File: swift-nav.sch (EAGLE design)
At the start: 197 parts, among them J1 SMA, J10 RF LINK, J2 6_PIN_100MIL, J3 DEBUG HDR, J4 PIN_HDR_EDG_1.27MM_5-2, J5 RF LINK, J6 ZX62-B-5PA, J7 C-GRID-02-70543, J8 CON_UART1, J9 CON_UART3, Q1 26MHz, Q2 DDTA143, Q3 2N7002, Q5 FDT458P, SW1 B3U-1000P, SW2 B3U-1000P, SW4 B3U-1000P, U1 6SLX9FTG256, U10 MAX2769, U11 SN74LVC07A_SOIC, U12 PT7M8206B33TA5EX, U13 M25PX80, U2 LTC3407A, U3 STM32-M-64-LQFP, U7 CC1110, U8 B4050, U9 B4050, X2 ASVTX-11

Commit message: Need to add different TCXO to schematic then ready for review
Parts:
- removed C25, C26, C27, C32, C34, C35, C46: 0.1uF, rcl:C-EUC0402
- removed C33, C58: 1uF, rcl:C-EUC0402
- removed C45: 0.01uF, rcl:C-EUC0402
- removed C56: 100uF, rcl:C-EUC1210K
- removed C57: 1pF, rcl:C-EUC0402
- removed C64: DNP, rcl:C-EUC0402
- removed C65: 1.5pF, rcl:C-EUC0402
- removed C68: 100pF, rcl:C-EUC0402
- removed C69, C70: 33pF, rcl:C-EUC0402
- removed C74: 1000pF, rcl:C-EUC0402
- removed D1: 1N581, jobygnss:1N581
- removed D2, D4: LED-0603, pel_dipol_comp:LED-0603
- removed D3, D6: LTST-C195KGJRKT, jobygnss:LTST-C195KGJRKT
- removed J10: RF LINK, pel_molex:CONN_4-1-53398
- removed J2: 6_PIN_100MIL, jobygnss:6_PIN_100MIL
- removed J9: CON_UART3, pel_molex:CONN_4-1-53398
- removed L12: 4.7uH, jobygnss:LQM2HPN4R7MG0L
- removed L4, L5: 12nH, pel_dipol_comp:INDUCTOR-0402
- removed L6, L7: 18nH, pel_dipol_comp:INDUCTOR-0402
- removed L8, L9: DNP, pel_dipol_comp:INDUCTOR-0402
- removed Q1: 26MHz, crystal:CRYSTALHC49UP
- removed Q2: DDTA143, transistor-pnp:MUN2111SOT23
- removed Q3: 2N7002, jobygnss:2N7002
- removed Q5: FDT458P, jobygnss:FDT458P
- removed R10, R58, R59, R9: 10k, rcl:R-US_R0402
- removed R19, R20, R40, R53, R57: 4K7, rcl:R-US_R0402
- removed R21, R22: 22R, pel_dipol_comp:RESISTOR-0402
- removed R23, R24: 0ohm/DNP, rcl:R-US_R0402
- removed R27: 1K5, pel_dipol_comp:RESISTOR-0402
- removed R29, R33: 0/DNP, pel_dipol_comp:RESISTOR-0402
- removed R31: 0R/DNP, rcl:R-US_R0402
- removed R32: 475K, rcl:R-US_R0402
- removed R37, R38, R50: 2k7, pel_dipol_comp:RESISTOR-0402
- removed R44, R46: 150, pel_dipol_comp:RESISTOR-0402
- removed R48: 56k, pel_dipol_comp:RESISTOR-0402
- removed R49: 270, pel_dipol_comp:RESISTOR-0402
- removed R51: 10k, pel_dipol_comp:RESISTOR-0402
- removed R66, R67, R68, R69: 10K, rcl:R-US_R0402
- removed SW1, SW2, SW4: B3U-1000P, jobygnss:B3U-1000P
- removed U11: SN74LVC07A_SOIC, jobygnss:SN74LVC07A_SOIC
- removed U7: CC1110, chipcon-ti-v2:CC1110
- removed X2: ASVTX-11, jobygnss:ASVTX-11
- added C15: DNP, rcl:C-EUC0402
- added LED1: RED, led:LEDCHIP-LED0603
- added LED2: GREEN, led:LEDCHIP-LED0603
- added X3: FPGA_DEBUG_HDR, pel_molex:CONN_12-1-53261
- C2: value DNP -> 0R
- J3: value DEBUG HDR -> SMA; device pel_misc:CONN_5-2-FTSH-V -> joby_robotics:SMA
- J5: value RF LINK -> CON_UART3
- R16: value 300 -> 330
- R17: value 4K7 -> 2K4
- R62: value 200K -> 140K
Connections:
- net MAX_NCS renamed SPI2NSS_MAX
- net N$42 renamed FPGA_INIT_B
- net SPI_CS renamed SPI2NSS_FLASH
- net SPI_MISO renamed SPI2MISO
- net SPI_MOSI renamed SPI2MOSI
- net SPI_SCK renamed SPI2SCK
- removed net 5VUSB: D1.A, J6.1, Q3.G, U3.PC0-ADC10
- removed net BATT_CHARGE_GATE: Q5.G, R57.1, U3.PC2-ADC12
- removed net FPGA_BUTT0: R53.2, SW4.2, U1B3.IO_L38N_M3DQ3_3
- removed net FPGA_BUTT1: R40.2, SW2.2, U1B3.IO_L39N_M3LDQSN_3
- removed net FPGA_CONF: R15.2, SW1.2, U1B2.PROGRAM_B_2, U3.PC12--USART3CK
- removed net FPGA_LED0: R46.2, U1B3.IO_L46N_M3CLKN_3
- removed net FPGA_LED1: R44.2, U1B3.IO_L40N_M3DQ7_3
- removed net FPGA_M0: R19.1, U1B2.IO_L1N_M0_CMPMISO_2
- removed net FPGA_M1: R20.2, U1B2.IO_L13P_M1_2
- removed net FPGA_TCK: J2.4, R69.2, U1BNA.TCK
- removed net FPGA_TDI: J2.2, R67.2, U1BNA.TDI
- removed net FPGA_TDO: J2.3, R68.2, U1BNA.TDO
- removed net FPGA_TMS: J2.1, R66.2, U1BNA.TMS
- removed net FT_USB_DM: J6.2, R21.1
- removed net LINK_RX: J10.1, J3.8, J5.4, U3.PC11--USART3RX, U7.P0.3
- removed net LINK_TX: J10.2, J3.10, J5.3, U3.PC10--USART3TX, U7.P0.2
- removed net MAX_CLKOUT: U11.5Y, U1B1.IO_L43N_GCLK4_M1DQ5_1
- removed net MAX_I0: U11.6Y, U1B1.IO_L48N_M1DQ9_1
- removed net MAX_I1: U11.1Y, U1B1.IO_L39N_M1ODT_1
- removed net MAX_Q0: U11.2Y, U1B1.IO_L53P_1
- removed net MAX_Q1: U11.3Y, U1B1.IO_L39P_M1A3_1
- removed net N$1: Q2.C, R27.2
- removed net N$12: Q3.D, R32.2
- removed net N$15: D4.C, U1B2.DONE_2
- removed net N$18: J9.2, R33.2
- removed net N$19: D6.2, R46.1
- removed net N$2: J8.2, R29.2
- removed net N$20: U10_DIG.CLKOUT, U11.5A
- removed net N$21: U10_DIG.Q1, U11.3A
- removed net N$23: D6.1, R44.1
- removed net N$25: L12.2, Q5.D, Q5.TAB
- removed net N$27: C45.1, R10.2, R9.1, X2.VCC
- removed net N$28: U10_DIG.I1, U11.1A
- removed net N$32: U10_DIG.I0, U11.6A
- removed net N$33: C57.2, C65.1, L5.2, L6.1
- removed net N$35: C33.1, U7.DCOUPL
- removed net N$36: C57.1, C58.1, L4.2, L7.1
- removed net N$37: L4.1, U7.RF-P
- removed net N$38: L5.1, U7.RF-N
- removed net N$40: C69.1, Q1.1, U7.XOSC1
- removed net N$41: D4.A, R16.1
- removed net N$43: C58.2, L6.2, L8.2
- removed net N$44: C64.1, L8.1, L9.2
- removed net N$47: C68.1, L7.2
- removed net N$48: C70.1, Q1.2, U7.XOSC2
- removed net N$49: R48.1, U7.RBIAS
- removed net N$50: D2.A, R49.1
- removed net N$51: C2.1, L9.1
- removed net N$52: C74.1, R50.2, U7.RESET
- removed net N$9: U10_DIG.Q0, U11.2A
- removed net P0_4-SSN: J3.5, U7.P0.4
- removed net P0_5-SCK: J3.6, U7.P0.5
- removed net P1_1-LED: R49.2, U7.P1.1
- removed net P2_1-DD: J3.4, U7.P2.1
- removed net P2_2-DC: J3.3, U7.P2.2
- removed net RESET_N: J3.7, R50.1, R51.1
- removed net SPI_FPGA_CS: U1B2.IO_L62N_D6_2, U3.PC8-TIM3CH3
- removed net TIM1CH1: U3.PA8-USART1CK/MCO/TIM1CH1
- removed net TIM2CH1: U1B3.IO_L49N_M3A2_3, U3.PA0-WKUP/USART2CTS/ADC0/TIM2CH1ETR
- removed net TIM4CH1: U1B3.IO_L48N_M3BA1_3, U3.PB6-I2C1SCL/TIM4CH1-USART1TX
- removed net UART2_RX: R36.2, U3.PA3-USART2RX/ADC3/TIM2CH4
- removed net USB_DISC: Q2.B, U3.PC15-OSC32_OUT
- removed net VBAT_MONITOR: R58.1, R59.2, U3.PC1-ADC11
- new net DEBUG0: X3.12
- new net DEBUG1: X3.11
- new net DEBUG10: X3.2
- new net DEBUG2: X3.10
- new net DEBUG3: X3.9
- new net DEBUG4: X3.8
- new net DEBUG5: X3.7
- new net DEBUG6: X3.6
- new net DEBUG7: X3.5
- new net DEBUG8: X3.4
- new net DEBUG9: X3.3
- new net FPGA_DONE: R16.1, U1B2.DONE_2
- new net FPGA_PROGRAM_B: R15.2, U1B2.PROGRAM_B_2, U3.PC12--USART3CK
- new net N$14: C15.2, C2.1, U9.2
- new net SPI1MISO: U1B3.IO_L40N_M3DQ7_3, U3.PA6-SPI1MISO/ADC6/TIM3CH1-TIM1BKIN
- new net SPI1MOSI: U1B3.IO_L39P_M3LDQS_3, U3.PA7-SPI1MOSI/ADC7/TIM3CH2-TIM1CH1N
- new net SPI1NSS: U1B3.IO_L40P_M3DQ6_3, U3.PA4-SPI1NSS/ADC4/USART2CK
- new net SPI1SCK: U1B3.IO_L41N_GCLK26_M3DQ5_3, U3.PA5-SPI1SCK/ADC5
- new net SPI2NSS_FPGA: U1B2.IO_L62N_D6_2
- new net STM_TDO_FPGA_TDI: U1BNA.TDI, U3.PB3/JTDO--TIM2CH2/TRACESWO/SPI1SCK
- new net TIM2CH1ETR: U1B1.IO_L43N_GCLK4_M1DQ5_1, U3.PA0-WKUP/USART2CTS/ADC0/TIM2CH1ETR
- new net TIM2CH2: U1B1.IO_L43P_GCLK5_M1DQ4_1, U3.PA1-USART2RTS/ADC1/TIM2CH2
- new net TIM2CH3: U1B1.IO_L44N_A2_M1DQ7_1, U3.PA2-USART2TX/ADC2/TIM2CH3
- new net TIM2CH4: U1B1.IO_L44P_A3_M1DQ6_1, U3.PA3-USART2RX/ADC3/TIM2CH4
- new net TIM3CH2: U1B1.IO_L39P_M1A3_1, U3.PC7-TIM3CH2
- new net TIM3CH3: U1B1.IO_L39N_M1ODT_1, U3.PC8-TIM3CH3
- new net TIM3CH4: U1B1.IO_L38P_A5_M1CLK_1, U3.PC9-TIM3CH4
- new net TIM3ETR: U1B1.IO_L38N_A4_M1CLKN_1, U3.PD2-TIM3ETR
- net +5V: now also J6.1, J7-1.S, J8.2; no longer D1.C, Q5.S, R29.1, R33.1
- net FE_CLK: no longer X2.OUT
- net FT_USB_DP: no longer R22.1
- net GND: now also C15.1, J3.2, J3.3, J3.4, J3.5, U1B2.IO_L13P_M1_2, X3.1; no longer C2.2, C25.2, C26.2, C27.2, C32.2, C33.2, C34.2, C35.2, C45.2, C46.2, C56.2, C64.2, C65.2, C68.2, C69.2, C70.2, C74.2, D2.C, D6.3, D6.4, J10.4, J2.5, J3.1, J9.1, Q3.S, R10.1, R20.1, R23.2, R24.1, R40.1, R48.2, R53.1, R59.1, SW1.1, U11.4A, U11.GND, U7.GND@1, X2.GND
- net JTAG_TCK: now also U1BNA.TCK
- net JTAG_TDO: now also U1BNA.TDO; no longer U3.PB3/JTDO--TIM2CH2/TRACESWO/SPI1SCK
- net JTAG_TMS: now also U1BNA.TMS
- net MAX_ANT_FLAG: no longer U3.PC9-TIM3CH4
- net MAX_LD: no longer U3.PD2-TIM3ETR
- net N$11: now also C2.2, C59.2, C75.2; no longer C75.1, U9.2
- net N$24: now also LED1.A; no longer D3.1
- net N$31: no longer R31.2
- net N$39: now also LED1.C; no longer D3.3
- net N$45: now also C75.1, J3.1; no longer C59.2, C75.2
- net N$53: no longer R32.1
- net N$55: now also LED2.A; no longer D3.2
- net N$59: now also LED2.C; no longer D3.4
- net TIM3CH1: now also U1B1.IO_L40N_GCLK10_M1A6_1; no longer U1B0.IO_L2P_0
- net UART3_RX: now also R36.2, U3.PC11--USART3RX; no longer J9.4, U1B3.IO_L34N_M3UDQSN_3
- net UART3_TX: now also U3.PC10--USART3TX; no longer J9.3, U1B3.IO_L35N_M3DQ11_3
- net USB_DM: now also J6.2; no longer R21.2, R37.2
- net USB_DP: no longer R22.2, R27.1, R38.2
- net V+: no longer J7-1.S, L12.1, R57.2, R58.2
- net VCC: no longer R9.2, X2.VDD
- net VCCIO: now also U1B2.IO_L1N_M0_CMPMISO_2; no longer C25.1, C26.1, C27.1, C32.1, C34.1, C35.1, C46.1, C56.1, J10.3, J2.6, J3.2, Q2.E, R19.2, R31.1, R37.1, R38.1, R51.2, R66.1, R67.1, R68.1, R69.1, SW2.1, SW4.1, U11.VCC, U7.AVDD-DREG, U7.AVDD@1, U7.AVDD@2, U7.AVDD@3, U7.AVDD@4, U7.DVDD@1, U7.DVDD@2, U7.GUARD
- net VSS1: no longer R23.1
- net VSS2: no longer R24.2
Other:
- note added: "3V3"
- note added: "5V Molex Connector"
- note added: "Digital 3V3 and 1V2"
- note added: "FPGA_DEBUG_HDR"
- note added: "JTAG chain"
- note added: "No STM32F10 compatibility"
- note added: "RF Frontend"
- note added: "SPARTAN6"
- note added: "TDI"
- note added: "TDO"
- note removed: "(Sets of 4 GCLK inputs go to the same buffer, eg 0-3, 4-7, etc)"
- note removed: "(all same bank, CLK_OUT to a GCLK)"
- note removed: "- Circuitry left to do :"
- note removed: "- Most signals to the Spartan6 can go to any Spartan 6 IO pin, just make sure clock lines"
- note removed: "- Please check footprints : some are from public libraries and I make a lot of footprint mistakes...."
- note removed: "- STM32 circuitry left to do :"
- note removed: "16MHZ_FPGA_OUT any pin / bank"
- note removed: "2V5"
- note removed: "All clock inputs (16MHZ_FPGA, 16MHZ_FPGA, MAX_CLK_OUT, SCLK)"
- note removed: "Battery charging"
- note removed: "Buffer should be outside RF can"
- note removed: "Check against LISA_M schematic"
- note removed: "Compatibility"
- note removed: "Digital 2V5 and 1V2"
- note removed: "Everything within this box should be on the breakoff portion of the board"
- note removed: "FPGA UART (same as LISA_M)"
- note removed: "GPS Frontend"
- note removed: "MAX signals to any pin / bank"
- note removed: "Notes"
- note removed: "Power"
- note removed: "Power Diodes from 5V connections (USB and UART headers)"
- note removed: "Pull ups / downs"
- note removed: "RF LINK"
- note removed: "RF Shields : MIS-208 and BMIS-202 (smaller?)"
- note removed: "Reset button"
- note removed: "STM32F20/10"
- note removed: "Timers / Interrupts to any pin / bank"
- note removed: "To molex"
- note removed: "UART1 (same as LISA_M)"
- note removed: "UART2 (same as LISA_M)"
- note removed: "USB (same as LISA_M)"
- note removed: "go to GCLKs and signals in a group go to the same bank (MAX, SPI, etc)"
- note removed: "should go to a different clock buffer"

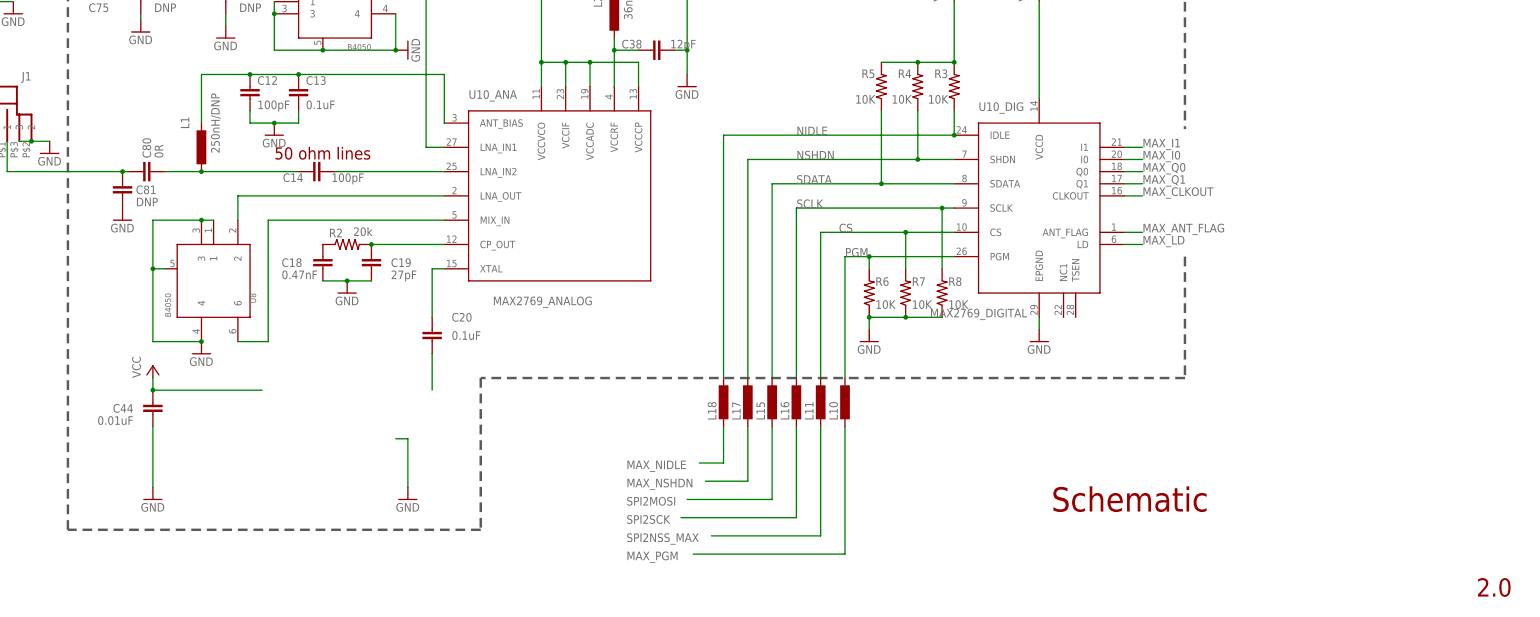
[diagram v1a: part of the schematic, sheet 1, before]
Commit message: Changed TXCO to TXC 7Q-16.368MBG-T (3v3, 16.368MHz, 0.5/2 2PPM TCXO) And added library with 7Q-16.368MBG-T package in it
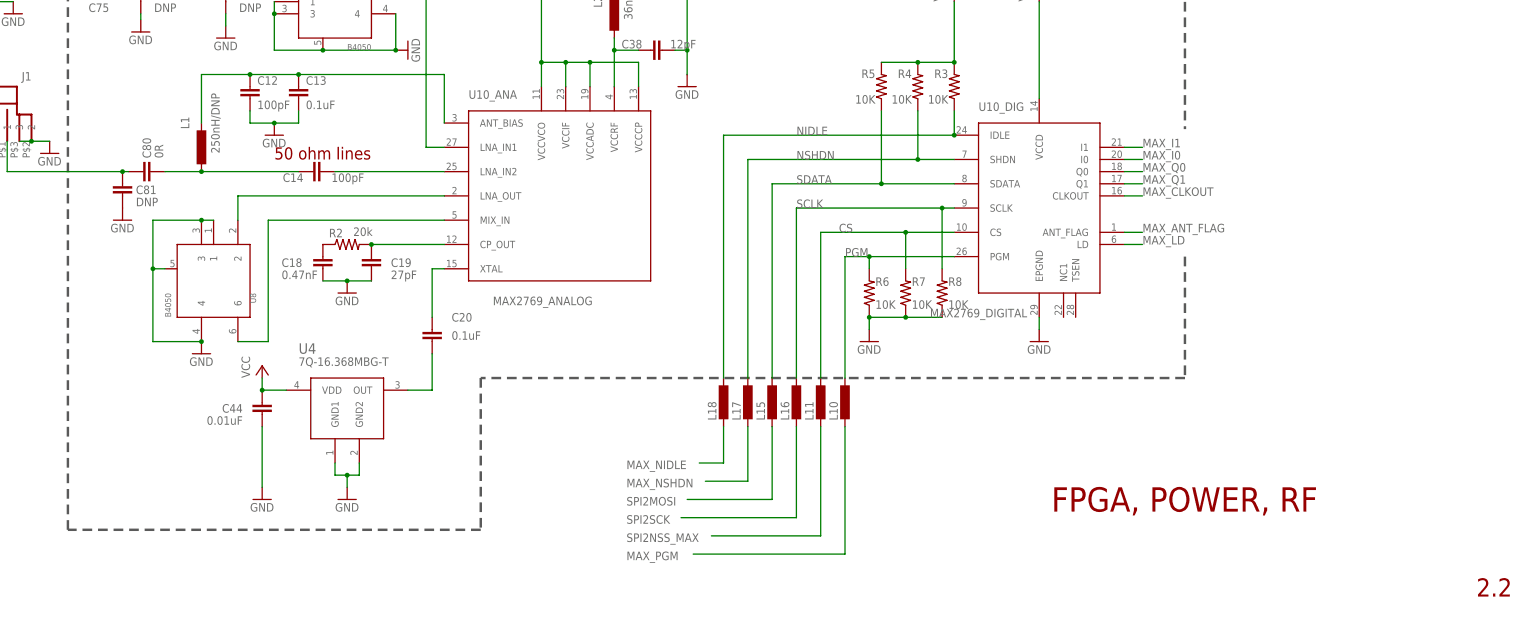
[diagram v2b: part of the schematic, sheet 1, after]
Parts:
- added U4: 7Q-16.368MBG-T, swift-nav:7Q-16.368MBG-T
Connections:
- net FE_CLK: now also U4.OUT
- net GND: now also U4.GND1, U4.GND2
- net VCC: now also U4.VDD
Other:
- note added: "2.2"
- note added: "FPGA, POWER, RF"
- note removed: "2.0"
- note removed: "Schematic"
- moved on the sheet: C44
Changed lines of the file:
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@@
 <setting verticaltext="up"/>
 </settings>
-<grid distance="0.05" unitdist="inch" unit="inch" style="lines" multiple="1" display="yes" altdistance="0.01" altunitdist="inch" altunit="inch"/>
+<grid distance="0.1" unitdist="inch" unit="inch" style="lines" multiple="1" display="no" altdistance="0.01" altunitdist="inch" altunit="inch"/>
 <layers>
 <layer number="1" name="Top" color="4" fill="1" visible="no" active="no"/>
@@
 <part name="GND39" library="supply1" deviceset="GND" device=""/>
 <part name="X3" library="pel_molex" deviceset="CONN_12-1" device="-53261" value="FPGA_DEBUG_HDR"/>
+<part name="U4" library="swift-nav" deviceset="7Q-16.368MBG-T" device=""/>
 </parts>
 <sheets>
@@
 <wire x1="248.92" y1="163.83" x2="482.6" y2="163.83" width="0.508" layer="97" style="shortdash"/>
 <wire x1="482.6" y1="163.83" x2="482.6" y2="107.95" width="0.508" layer="97" style="shortdash"/>
-<text x="543.56" y="10.16" size="3.81" layer="94">2.0</text>
+<text x="543.56" y="10.16" size="3.81" layer="94">2.2</text>
 <text x="78.74" y="401.32" size="6.4516" layer="94">Spartan Configuration</text>
 <text x="346.71" y="168.91" size="6.4516" layer="94">RF Frontend</text>
 <text x="297.18" y="410.21" size="6.4516" layer="94">Spartan IO Banks</text>
-<text x="454.66" y="27.94" size="5.08" layer="94">Schematic</text>
+<text x="454.66" y="27.94" size="5.08" layer="94">FPGA, POWER, RF</text>
 <text x="292.1" y="147.32" size="2.54" layer="94">50 ohm lines</text>
 <text x="292.1" y="101.6" size="2.54" layer="94">50 ohm lines</text>
@@
 </instance>
 <instance part="GND28" gate="1" x="416.56" y="63.5"/>
-<instance part="C44" gate="G$1" x="266.7" y="50.8" smashed="yes">
-<attribute name="NAME" x="262.636" y="50.419" size="1.778" layer="95" rot="R180"/>
-<attribute name="VALUE" x="262.636" y="47.879" size="1.778" layer="96" rot="R180"/>
+<instance part="C44" gate="G$1" x="289.56" y="50.8" smashed="yes">
+<attribute name="NAME" x="285.496" y="50.419" size="1.778" layer="95" rot="R180"/>
+<attribute name="VALUE" x="285.496" y="47.879" size="1.778" layer="96" rot="R180"/>
 </instance>
-<instance part="GND30" gate="1" x="266.7" y="30.48"/>
-<instance part="GND32" gate="1" x="320.04" y="30.48"/>
+<instance part="GND30" gate="1" x="289.56" y="30.48"/>
+<instance part="GND32" gate="1" x="307.34" y="30.48"/>
 <instance part="FRAME2" gate="G$1" x="0" y="0"/>
 <instance part="FRAME2" gate="G$2" x="452.12" y="2.54"/>
@@
 <instance part="U1" gate="BVCCAUX" x="53.34" y="76.2"/>
 <instance part="U1" gate="BVCCINT" x="76.2" y="76.2"/>
-<instance part="U10" gate="_ANA" x="332.74" y="76.2"/>
+<instance part="U10" gate="_ANA" x="332.74" y="76.2" smashed="yes">
+<attribute name="NAME" x="332.74" y="114.3" size="1.778" layer="95"/>
+</instance>
 <instance part="U10" gate="_DIG" x="439.42" y="73.66"/>
 <instance part="VCC4" gate="G$1" x="60.96" y="91.44"/>
@@
 <instance part="VCC7" gate="G$1" x="119.38" y="71.12"/>
 <instance part="P+2" gate="VCC" x="121.92" y="123.19"/>
-<instance part="P+3" gate="VCC" x="266.7" y="58.42"/>
+<instance part="P+3" gate="VCC" x="289.56" y="58.42"/>
 <instance part="P+4" gate="VCC" x="347.98" y="152.4"/>
 <instance part="P+5" gate="VCC" x="363.22" y="152.4"/>
@@
 <instance part="GND39" gate="1" x="472.44" y="294.64"/>
 <instance part="X3" gate="G$1" x="483.87" y="313.69"/>
+<instance part="U4" gate="U$1" x="307.34" y="50.8"/>
 </instances>
 <busses>
@@
 </segment>
 <segment>
-<wire x1="266.7" y1="33.02" x2="266.7" y2="45.72" width="0.1524" layer="91"/>
+<wire x1="289.56" y1="33.02" x2="289.56" y2="45.72" width="0.1524" layer="91"/>
 <pinref part="C44" gate="G$1" pin="2"/>
 <pinref part="GND30" gate="1" pin="GND"/>
 </segment>
 <segment>
-<wire x1="317.5" y1="43.18" x2="320.04" y2="43.18" width="0.1524" layer="91"/>
-<wire x1="320.04" y1="43.18" x2="320.04" y2="33.02" width="0.1524" layer="91"/>
-<pinref part="GND32" gate="1" pin="GND"/>
-</segment>
-<segment>
 <wire x1="30.48" y1="83.82" x2="33.02" y2="83.82" width="0.1524" layer="91"/>
 <wire x1="33.02" y1="81.28" x2="33.02" y2="83.82" width="0.1524" layer="91"/>
@@
 <pinref part="X3" gate="G$1" pin="1"/>
 </segment>
+<segment>
+<pinref part="U4" gate="U$1" pin="GND1"/>
+<wire x1="304.8" y1="38.1" x2="304.8" y2="35.56" width="0.1524" layer="91"/>
+<pinref part="U4" gate="U$1" pin="GND2"/>
+<wire x1="304.8" y1="35.56" x2="307.34" y2="35.56" width="0.1524" layer="91"/>
+<wire x1="307.34" y1="35.56" x2="309.88" y2="35.56" width="0.1524" layer="91"/>
+<wire x1="309.88" y1="35.56" x2="309.88" y2="38.1" width="0.1524" layer="91"/>
+<pinref part="GND32" gate="1" pin="GND"/>
+<wire x1="307.34" y1="33.02" x2="307.34" y2="35.56" width="0.1524" layer="91"/>
+<junction x="307.34" y="35.56"/>
+</segment>
 </net>
 <net name="N$3" class="0">
@@
 <wire x1="325.12" y1="53.34" x2="325.12" y2="60.96" width="0.1524" layer="91"/>
 <pinref part="C20" gate="G$1" pin="2"/>
+<pinref part="U4" gate="U$1" pin="OUT"/>
+<wire x1="320.04" y1="53.34" x2="325.12" y2="53.34" width="0.1524" layer="91"/>
 </segment>
 </net>
@@
 </segment>
 <segment>
-<wire x1="266.7" y1="55.88" x2="266.7" y2="53.34" width="0.1524" layer="91"/>
-<wire x1="266.7" y1="53.34" x2="289.56" y2="53.34" width="0.1524" layer="91"/>
-<junction x="266.7" y="53.34"/>
+<wire x1="289.56" y1="55.88" x2="289.56" y2="53.34" width="0.1524" layer="91"/>
+<wire x1="289.56" y1="53.34" x2="294.64" y2="53.34" width="0.1524" layer="91"/>
+<junction x="289.56" y="53.34"/>
 <pinref part="C44" gate="G$1" pin="1"/>
 <pinref part="P+3" gate="VCC" pin="VCC"/>
+<pinref part="U4" gate="U$1" pin="VDD"/>
 </segment>
 <segment>
@@
 <text x="20.32" y="384.81" size="3.81" layer="94">5V Molex Connector</text>
 <text x="24.13" y="269.24" size="3.81" layer="91" rot="MR180">UART3</text>
-<text x="118.11" y="162.56" size="3.81" layer="91" rot="MR180">JTAG chain</text>
-<rectangle x1="114.3" y1="134.62" x2="127" y2="146.05" layer="91"/>
-<rectangle x1="137.16" y1="134.62" x2="149.86" y2="146.05" layer="91"/>
-<text x="96.52" y="138.43" size="2.54" layer="91">TDI</text>
-<text x="95.25" y="125.73" size="2.54" layer="91">TDO</text>
-<text x="115.57" y="148.59" size="2.54" layer="91">STM32</text>
-<text x="134.62" y="148.59" size="2.54" layer="91">SPARTAN6</text>
+<text x="100.33" y="154.94" size="3.81" layer="91" rot="MR180">JTAG chain</text>
+<rectangle x1="96.52" y1="127" x2="109.22" y2="138.43" layer="91"/>
+<rectangle x1="119.38" y1="127" x2="132.08" y2="138.43" layer="91"/>
+<text x="78.74" y="130.81" size="2.54" layer="91">TDI</text>
+<text x="77.47" y="118.11" size="2.54" layer="91">TDO</text>
+<text x="97.79" y="140.97" size="2.54" layer="91">STM32</text>
+<text x="116.84" y="140.97" size="2.54" layer="91">SPARTAN6</text>
 </plain>
 <instances>
@@
 <net name="N$1" class="0">
 <segment>
-<wire x1="104.14" y1="139.7" x2="114.3" y2="139.7" width="0.1524" layer="91"/>
+<wire x1="86.36" y1="132.08" x2="96.52" y2="132.08" width="0.1524" layer="91"/>
 </segment>
 </net>
 <net name="N$2" class="0">
 <segment>
-<wire x1="104.14" y1="127" x2="114.3" y2="127" width="0.1524" layer="91"/>
+<wire x1="86.36" y1="119.38" x2="96.52" y2="119.38" width="0.1524" layer="91"/>
 </segment>
 </net>
 <net name="N$12" class="0">
 <segment>
-<wire x1="127" y1="139.7" x2="137.16" y2="139.7" width="0.1524" layer="91"/>
+<wire x1="109.22" y1="132.08" x2="119.38" y2="132.08" width="0.1524" layer="91"/>
 </segment>
 </net>
 <net name="N$13" class="0">
 <segment>
-<wire x1="149.86" y1="139.7" x2="156.21" y2="139.7" width="0.1524" layer="91"/>
-<wire x1="156.21" y1="139.7" x2="156.21" y2="127" width="0.1524" layer="91"/>
-<wire x1="156.21" y1="127" x2="114.3" y2="127" width="0.1524" layer="91"/>
+<wire x1="132.08" y1="132.08" x2="138.43" y2="132.08" width="0.1524" layer="91"/>
+<wire x1="138.43" y1="132.08" x2="138.43" y2="119.38" width="0.1524" layer="91"/>
+<wire x1="138.43" y1="119.38" x2="96.52" y2="119.38" width="0.1524" layer="91"/>
 </segment>
 </net>

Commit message: Rearranged schematic a bit and cleared up some errors
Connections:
- new net MAX_CLKOUT: U10_DIG.CLKOUT, U1B0.IO_L37P_GCLK13_0
- new net MAX_I0: U10_DIG.I0, U1B0.IO_L39N_0
- new net MAX_I1: U10_DIG.I1, U1B0.IO_L39P_0
- new net MAX_Q0: U10_DIG.Q0, U1B0.IO_L38N_VREF_0
- new net MAX_Q1: U10_DIG.Q1, U1B0.IO_L38P_0
- net DEBUG0: now also U1B3.IO_L32N_M3DQ15_3
- net DEBUG1: now also U1B3.IO_L32P_M3DQ14_3
- net DEBUG10: now also U1B3.IO_L37N_M3DQ1_3
- net DEBUG2: now also U1B3.IO_L33N_M3DQ13_3
- net DEBUG3: now also U1B3.IO_L33P_M3DQ12_3
- net DEBUG4: now also U1B3.IO_L34N_M3UDQSN_3
- net DEBUG5: now also U1B3.IO_L34P_M3UDQS_3
- net DEBUG6: now also U1B3.IO_L35N_M3DQ11_3
- net DEBUG7: now also U1B3.IO_L35P_M3DQ10_3
- net DEBUG8: now also U1B3.IO_L36N_M3DQ9_3
- net DEBUG9: now also U1B3.IO_L36P_M3DQ8_3
- net FPGA_DONE: now also U3.PC1-ADC11
- net FPGA_INIT_B: now also U3.PC0-ADC10
- net MAX_ANT_FLAG: now also U3.PC5-ADC15
- net MAX_LD: now also U3.PA8-USART1CK/MCO/TIM1CH1
- net SPI2NSS_FPGA: now also U3.PC2-ADC12
- net UART3_RX: now also J5.4
- net UART3_TX: now also J5.3
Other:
- note added: "FPGA / POWER / RF"
- note added: "STM32 / CONNECTORS"
- note removed: "Analog 3V3"
- note removed: "FPGA, POWER, RF"
- note removed: "MAX2769 Bypass"
- moved on the sheet: ANT1, C1, C10, C11, C12, C13, C14, C15, C18, C19, C2, C20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

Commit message: Some changes post schematic review, more to come... Removed FPGA_D1_MISO2 and FPGA_D2_MISO3, changed R12 and R11 to hard shorts to VCCIO Removed Molex connector Replaced all +5V power symbols with V+ Removed SAW filter between Patch and LNA1 input Removed pull ups on MAX digital signals Removed ferrites from MAX digital signals Removed pull down from STM BOOT0 and shorted BOOT0 to GND Removed pull ups from UART1_RX and UART3_RX Renamed "FT_USB_DP" to "USB_DP" (wasn't connected, old net name from when 22 ohm series resistors were there) Renamed "16MHZ_CLK_OUT" to "STM_CLK_IN"
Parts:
- removed J7: C-GRID-02-70543, jobygnss:C-GRID-02-70543
- removed L10, L11, L15, L16, L17, L18: (no value), pel_dipol_comp:INDUCTOR-0402
- removed R11, R12: 100k, rcl:R-US_R0402
- removed R3, R4, R5, R6, R7, R8: 10K, rcl:R-US_R0402
- removed R35, R36, R43: 2k7, pel_dipol_comp:RESISTOR-0402
- removed U9: B4050, jobygnss:B4050
- added C16: 0R, rcl:C-EUC0402
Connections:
- net 16MHZ_FPGA_OUT renamed STM_CLK_IN
- removed net +5V: J6.1, J7-1.S, J8.2
- removed net BOOT0: R43.2, U3.BOOT0
- removed net CS: L11.1, R7.2, U10_DIG.CS
- removed net FPGA_D1_MISO2: R12.1, U13.NWP, U1B2.IO_L12P_D1_MISO2_2
- removed net FPGA_D2_MISO3: R11.1, U13.NHOLD, U1B2.IO_L12N_D2_MISO3_2
- removed net FT_USB_DP: J6.3
- removed net N$14: C15.2, C2.1, U9.2
- removed net NIDLE: L18.1, R3.1, U10_DIG.IDLE
- removed net PGM: L10.1, R6.2, U10_DIG.PGM
- removed net SCLK: L16.1, R8.2, U10_DIG.SCLK
- removed net SDATA: L15.1, R5.1, U10_DIG.SDATA
- new net N$9: C15.2, C16.1, C75.1
- net GND: now also U3.BOOT0; no longer J7-2.S, R43.1, R6.1, R7.1, R8.1, U9.1, U9.3, U9.4, U9.5
- net MAX_NIDLE: now also U10_DIG.IDLE; no longer L18.2
- net MAX_NSHDN: no longer L17.2
- net MAX_PGM: now also U10_DIG.PGM; no longer L10.2
- net N$29: now also C2.1; no longer U9.6
- net N$45: now also C16.2; no longer C75.1
- net NSHDN: no longer L17.1, R4.1
- net SPI2MOSI: now also U10_DIG.SDATA; no longer L15.2
- net SPI2NSS_MAX: now also U10_DIG.CS; no longer L11.2
- net SPI2SCK: now also U10_DIG.SCLK; no longer L16.2
- net UART1_RX: no longer R35.2
- net UART3_RX: no longer R36.2
- net USB_DP: now also J6.3
- net V+: now also J6.1, J8.2
- net VCC: no longer R3.2, R4.2, R5.2
- net VCCIO: now also U13.NHOLD, U13.NWP; no longer R11.2, R12.2, R35.1, R36.1
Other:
- note added: "Inner RF Shield"
- note added: "Outer RF shield"
- note removed: "5V Molex Connector"
- moved on the sheet: ANT1, C15, C18, C19, C2, C20, C21, C22, C23, C24, C28, C29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
